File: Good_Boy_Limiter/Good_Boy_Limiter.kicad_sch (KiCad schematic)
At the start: 37 parts, among them J2 Extra General Pins, Q2 AO3422, SW3 RESET1, SW4 BOOT1, U1 ESP32-S3-WROOM-1, U2 TC4427EOA_C636891, U3 LM2576HVR-12, U8 B3B-XH-A, U9 LM393DR2G

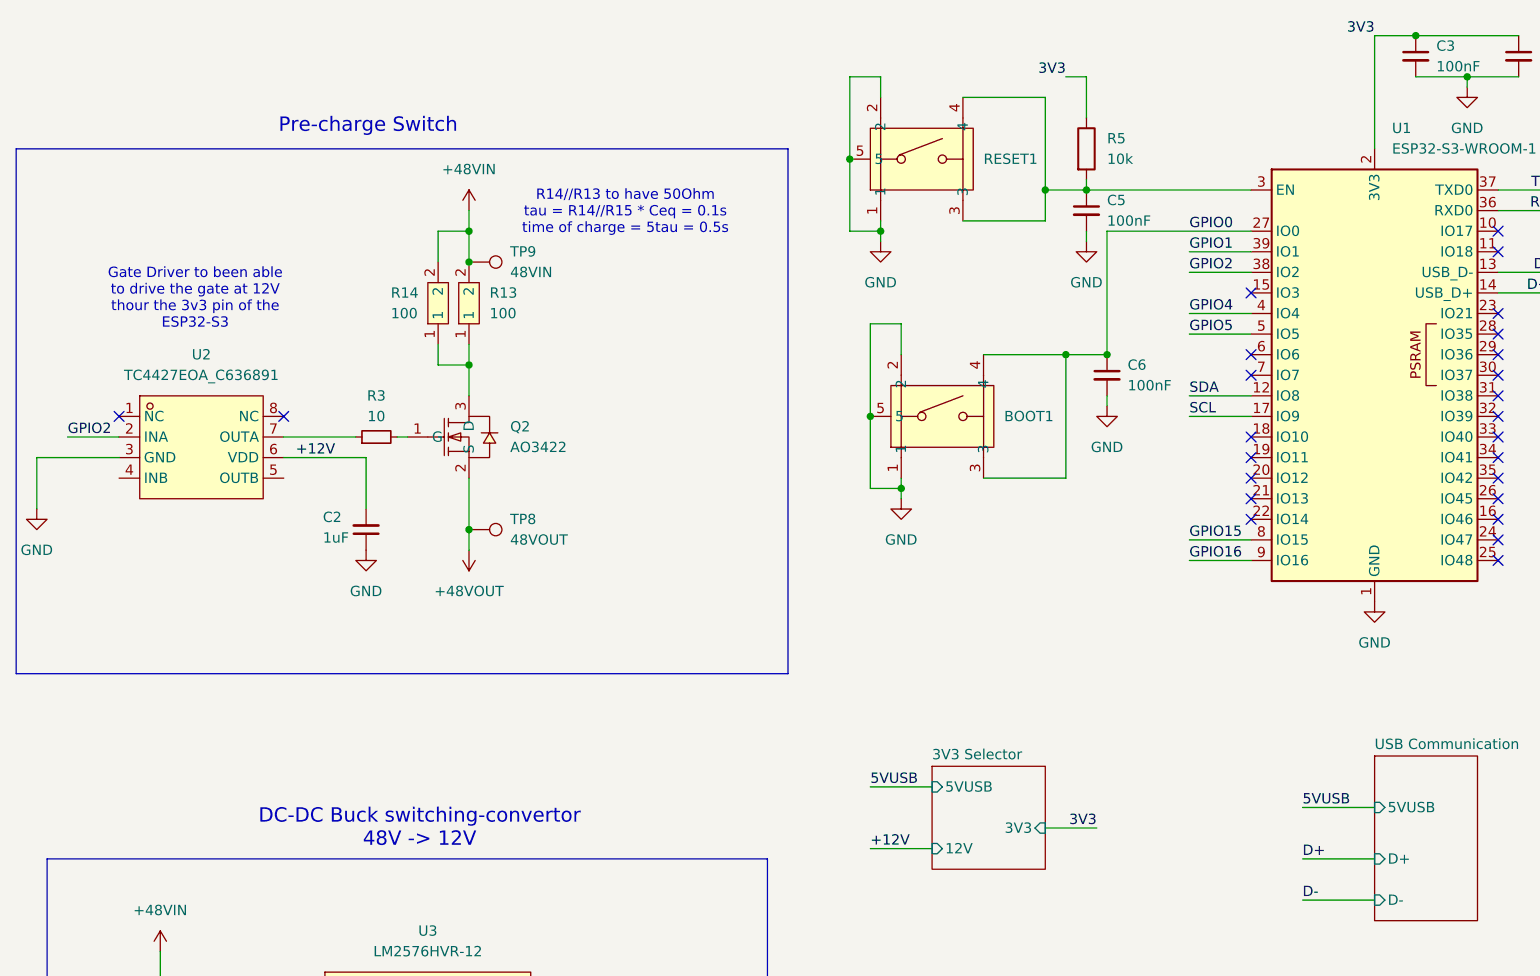
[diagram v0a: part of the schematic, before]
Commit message: Added PWR-FLag for ERC check
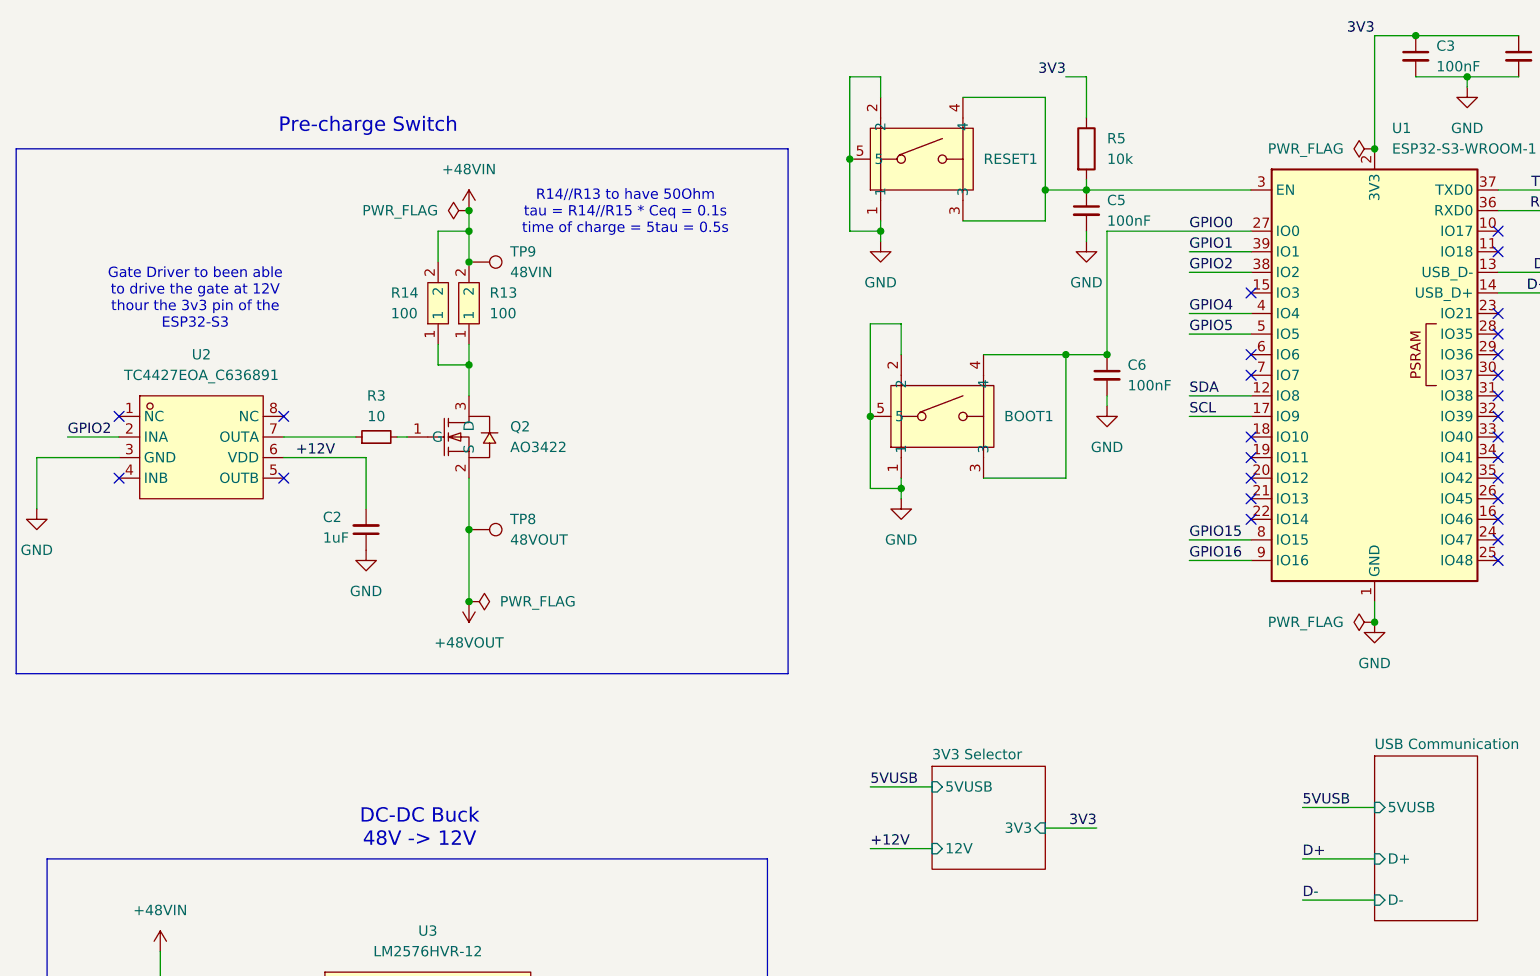
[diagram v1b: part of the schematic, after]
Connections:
- no-connect marks 26 -> 28
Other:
- note added: "DC-DC Buck 48V -> 12V"
- note removed: "DC-DC Buck switching-convertor 48V -> 12V"

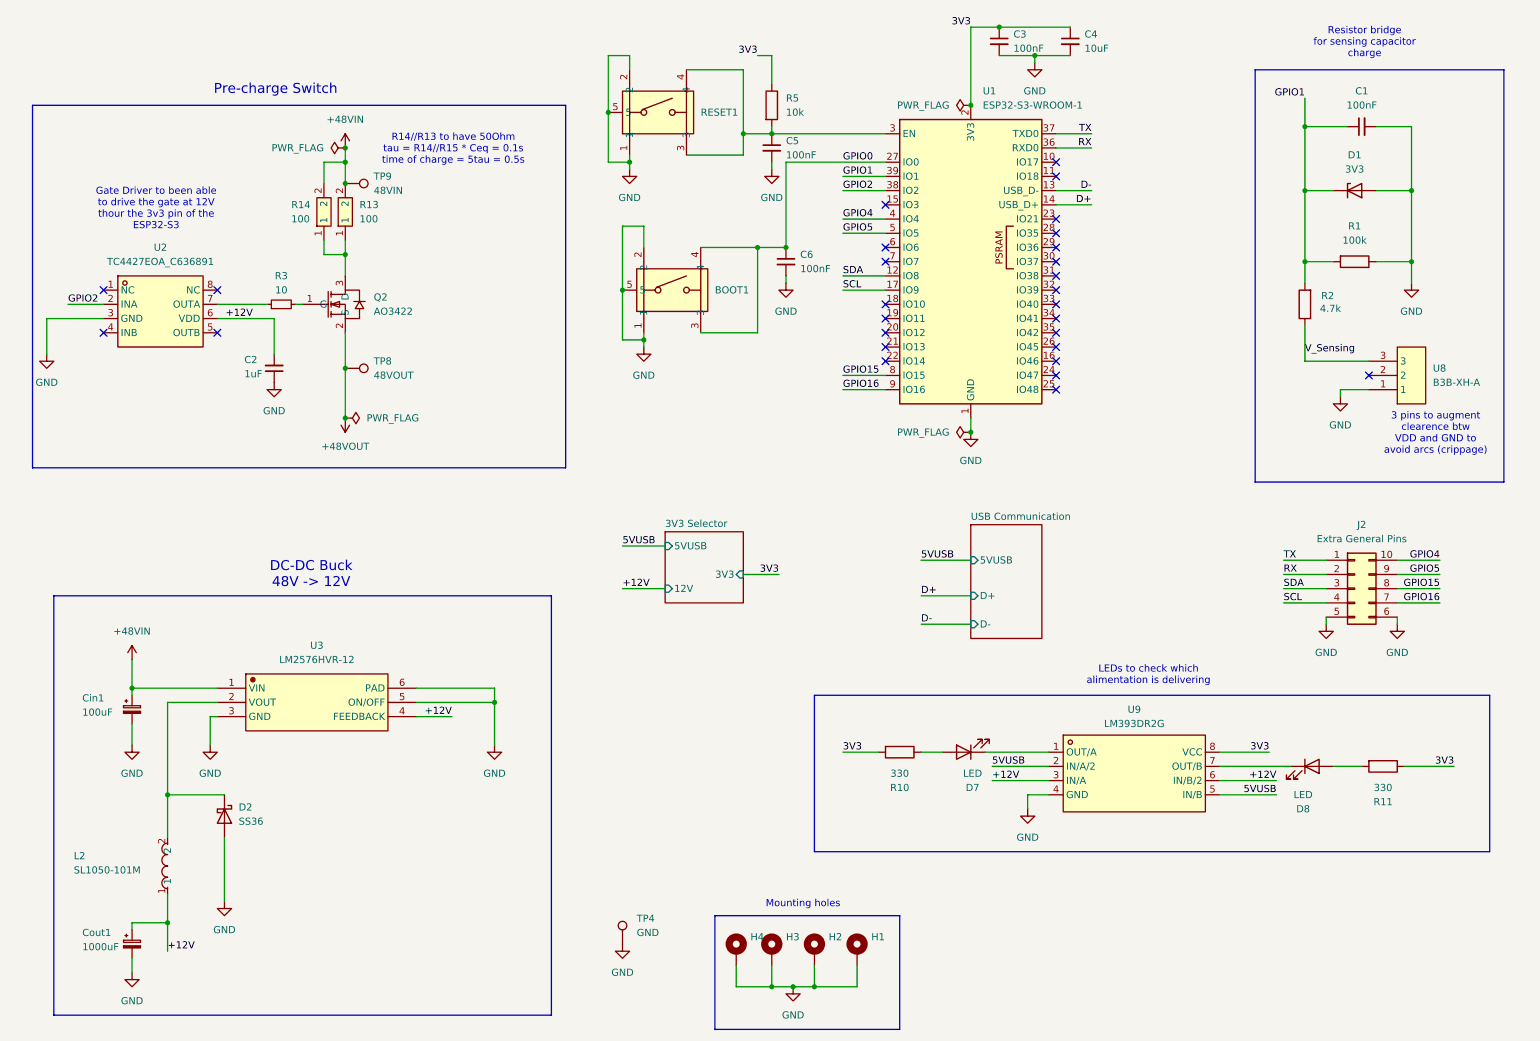
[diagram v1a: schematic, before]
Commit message: fix: added 4 voltage sensing modules to measure all the 4 PDBs
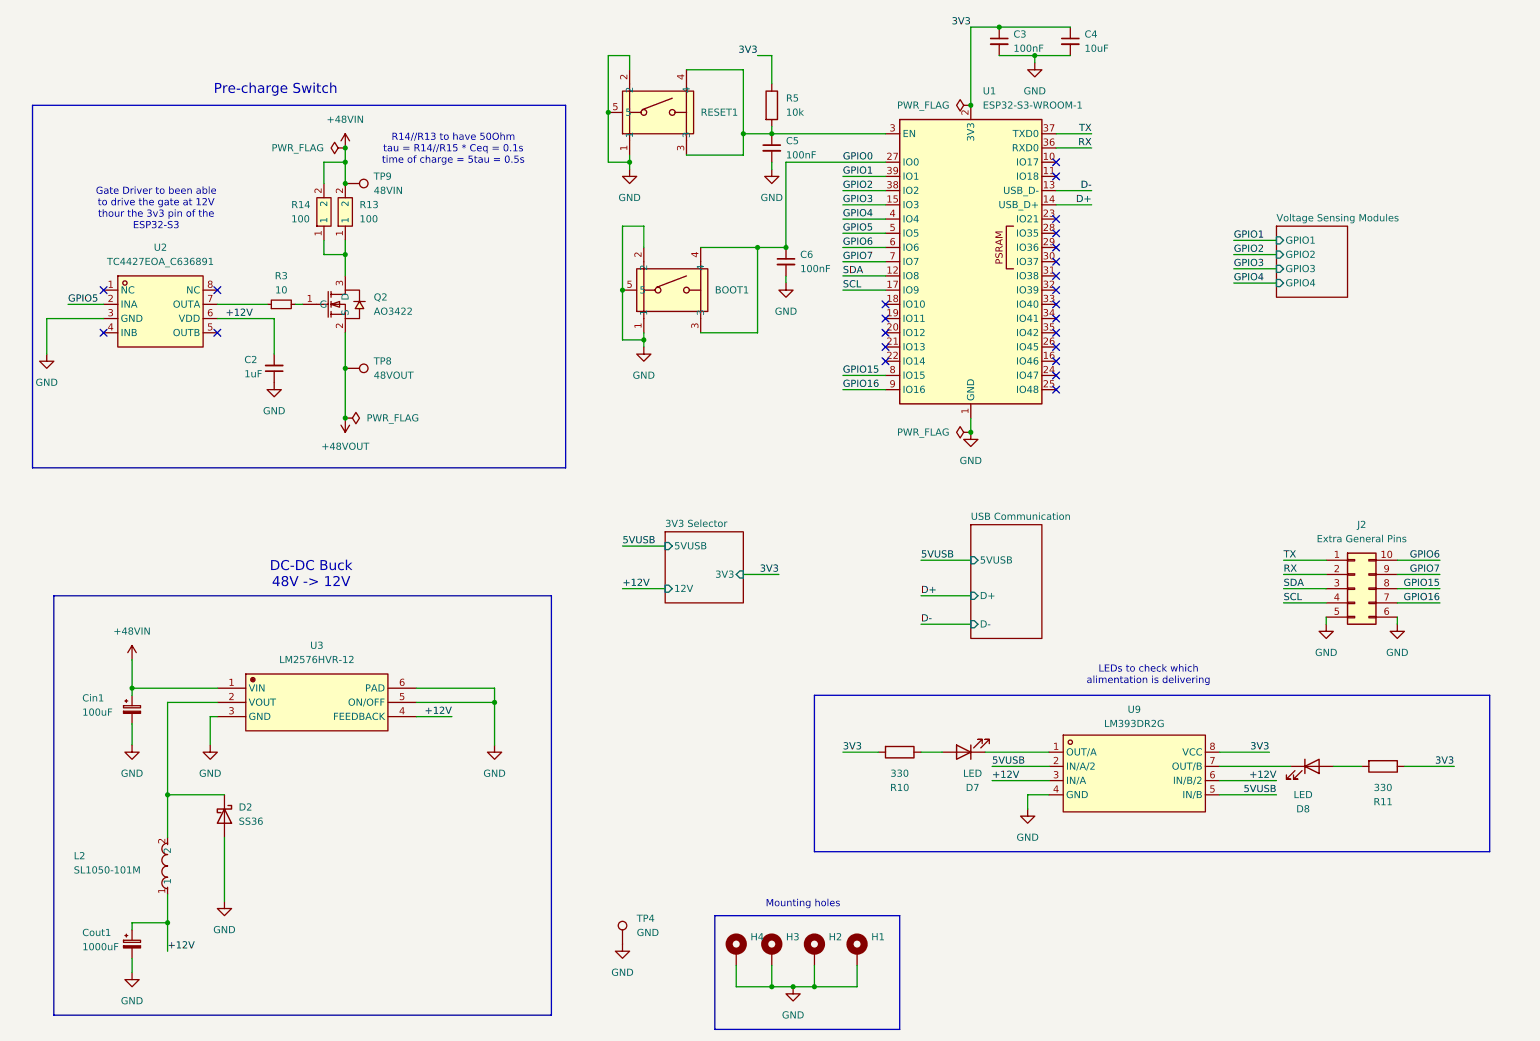
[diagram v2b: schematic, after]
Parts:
- removed C1: 100nF, Capacitor_SMD:C_0201_0603Metric_Pad0.64x0.40mm_HandSolder, symbol Device:C_Small
- removed D1: 3V3, Package_TO_SOT_SMD:SOT-23, symbol Diode:BZX84Cxx
- removed R1: 100k, Resistor_SMD:R_0603_1608Metric_Pad0.98x0.95mm_HandSolder, symbol Device:R
- removed R2: 4.7k, Resistor_SMD:R_0603_1608Metric_Pad0.98x0.95mm_HandSolder, symbol Device:R
- removed U8: B3B-XH-A, easyeda2kicad:CONN-TH_3P-P2.50_A2501WV2-3P, symbol easyeda2kicad:B3B-XH-A
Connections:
- net GPIO2: no longer U2.2 (INA)
- net GPIO4: no longer J2.10 (Pin_10)
- net GPIO5: now also U2.2 (INA); no longer J2.9 (Pin_9)
- net GPIO3: now reaches U1.15 (IO3)
- net GPIO6: now reaches U1.6 (IO6)
- net GPIO6: now also J2.10 (Pin_10)
- net GPIO7: now reaches U1.7 (IO7)
- net GPIO7: now also J2.9 (Pin_9)
- no-connect marks 28 -> 24
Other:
- added sheet Voltage Sensing Modules (vsensing_modules.kicad_sch)
- note removed: "3 pins to augment clearence btw VDD and GND to avoid arcs (crippage)"
- note removed: "Resistor bridge for sensing capacitor charge"

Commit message: Routing update
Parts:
- added R19, R20: 22, Resistor_SMD:R_0402_1005Metric, symbol Device:R_Small
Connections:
- net D+: now also R20.2; no longer U1.14 (USB_D+)
- net D-: now also R19.2; no longer U1.13 (USB_D-)
- new net: R19.1, U1.13 (USB_D-)
- new net: R20.1, U1.14 (USB_D+)
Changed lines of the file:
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@@
 	(wire
 		(pts
-			(xy 200.66 46.99) (xy 207.01 46.99)
+			(xy 200.66 46.99) (xy 209.55 46.99)
 		)
 		(stroke
@@
 	(wire
 		(pts
-			(xy 200.66 49.53) (xy 207.01 49.53)
+			(xy 200.66 49.53) (xy 209.55 49.53)
 		)
 		(stroke
@@
 	(wire
 		(pts
+			(xy 220.98 46.99) (xy 214.63 46.99)
+		)
+		(stroke
+			(width 0)
+			(type default)
+		)
+	)
+	(wire
+		(pts
 			(xy 137.16 57.15) (xy 147.32 57.15)
 		)
@@
 	(wire
 		(pts
+			(xy 220.98 49.53) (xy 214.63 49.53)
+		)
+		(stroke
+			(width 0)
+			(type default)
+		)
+	)
+	(wire
+		(pts
 			(xy 152.4 62.23) (xy 152.4 63.5)
 		)
@@
 		)
 	)
-	(label "D-"
-		(at 207.01 46.99 180)
-		(effects
-			(font
-				(size 1.27 1.27)
-			)
-			(justify right bottom)
-		)
-	)
 	(label "GPIO0"
 		(at 162.56 41.91 0)
@@
 		)
 	)
+	(label "D-"
+		(at 220.98 46.99 180)
+		(effects
+			(font
+				(size 1.27 1.27)
+			)
+			(justify right bottom)
+		)
+	)
 	(label "+12V"
 		(at 41.91 182.88 0)
@@
 		)
 	)
+	(label "D+"
+		(at 220.98 49.53 180)
+		(effects
+			(font
+				(size 1.27 1.27)
+			)
+			(justify right bottom)
+		)
+	)
 	(label "5VUSB"
 		(at 176.53 113.03 0)
@@
 		)
 	)
-	(label "D+"
-		(at 207.01 49.53 180)
-		(effects
-			(font
-				(size 1.27 1.27)
-			)
-			(justify right bottom)
-		)
-	)
 	(label "GPIO6"
 		(at 269.24 113.03 180)
@@
 	)
 	(symbol
+		(lib_id "Device:R_Small")
+		(at 212.09 46.99 90)
+		(unit 1)
+		(exclude_from_sim no)
+		(in_bom yes)
+		(on_board yes)
+		(dnp no)
+		(fields_autoplaced yes)
+		(property "Reference" "R19"
+			(at 212.09 41.91 90)
+			(effects
+				(font
+					(size 1.27 1.27)
+				)
+			)
+		)
+		(property "Value" "22"
+			(at 212.09 44.45 90)
+			(effects
+				(font
+					(size 1.27 1.27)
+				)
+			)
+		)
+		(property "Footprint" "Resistor_SMD:R_0402_1005Metric"
+			(at 212.09 46.99 0)
+			(effects
+				(font
+					(size 1.27 1.27)
+				)
+				(hide yes)
+			)
+		)
+		(property "Datasheet" "~"
+			(at 212.09 46.99 0)
+			(effects
+				(font
+					(size 1.27 1.27)
+				)
+				(hide yes)
+			)
+		)
+		(property "Description" "Resistor, small symbol"
+			(at 212.09 46.99 0)
+			(effects
+				(font
+					(size 1.27 1.27)
+				)
+				(hide yes)
+			)
+		)
+		(property "LCSC Part" "C174144"
+			(at 212.09 46.99 0)
+			(effects
+				(font
+					(size 1.27 1.27)
+				)
+				(hide yes)
+			)
+		)
+		(pin "1"
+		)
+		(pin "2"
+		)
+		(instances
+			(project "Good_Boy_Limiter"
+				(path "/e6249df1-5b78-4b75-b804-4c6c30b1afc2"
+					(reference "R19")
+					(unit 1)
+				)
+			)
+		)
+	)
+	(symbol
 		(lib_id "power:GND")
 		(at 127 74.93 0)
@@
 					(unit 1)
 				)
+			)
+		)
+	)
+	(symbol
+		(lib_id "Device:R_Small")
+		(at 212.09 49.53 90)
+		(unit 1)
+		(exclude_from_sim no)
+		(in_bom yes)
+		(on_board yes)
+		(dnp no)
+		(property "Reference" "R20"
+			(at 212.09 52.07 90)
+			(effects
+				(font
+					(size 1.27 1.27)
+				)
+			)
+		)
+		(property "Value" "22"
+			(at 212.09 54.61 90)
+			(effects
+				(font
+					(size 1.27 1.27)
+				)
+			)
+		)
+		(property "Footprint" "Resistor_SMD:R_0402_1005Metric"
+			(at 212.09 49.53 0)
+			(effects
+				(font
+					(size 1.27 1.27)
+				)
+				(hide yes)
+			)
+		)
+		(property "Datasheet" "~"
+			(at 212.09 49.53 0)
+			(effects
+				(font
+					(size 1.27 1.27)
+				)
+				(hide yes)
+			)
+		)
+		(property "Description" "Resistor, small symbol"
+			(at 212.09 49.53 0)
+			(effects
+				(font
+					(size 1.27 1.27)
+				)
+				(hide yes)
+			)
+		)
+		(property "LCSC Part" "C174144"
+			(at 212.09 49.53 0)
+			(effects
+				(font
+					(size 1.27 1.27)
+				)
+				(hide yes)
+			)
+		)
+		(pin "1"
+		)
+		(pin "2"
+		)
+		(instances
+			(project "Good_Boy_Limiter"
+				(path "/e6249df1-5b78-4b75-b804-4c6c30b1afc2"
+					(reference "R20")
+					(unit 1)
+				)

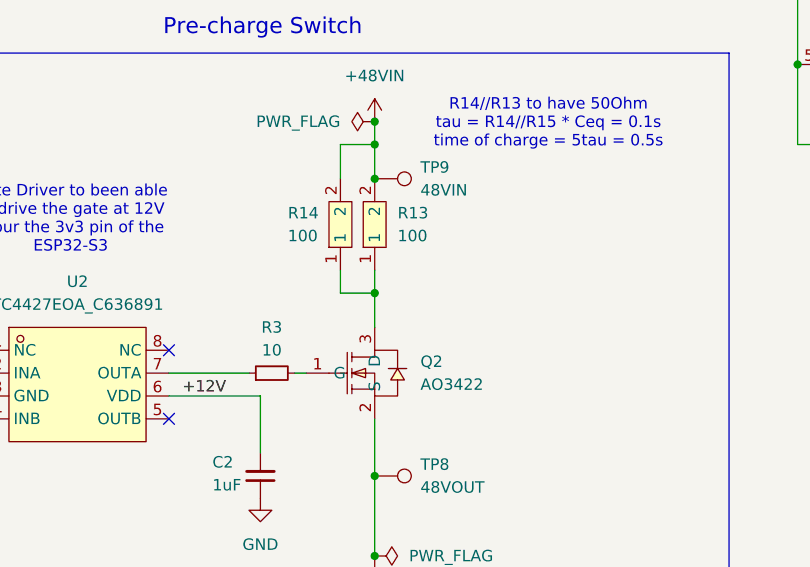
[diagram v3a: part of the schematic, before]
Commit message: More update on routing
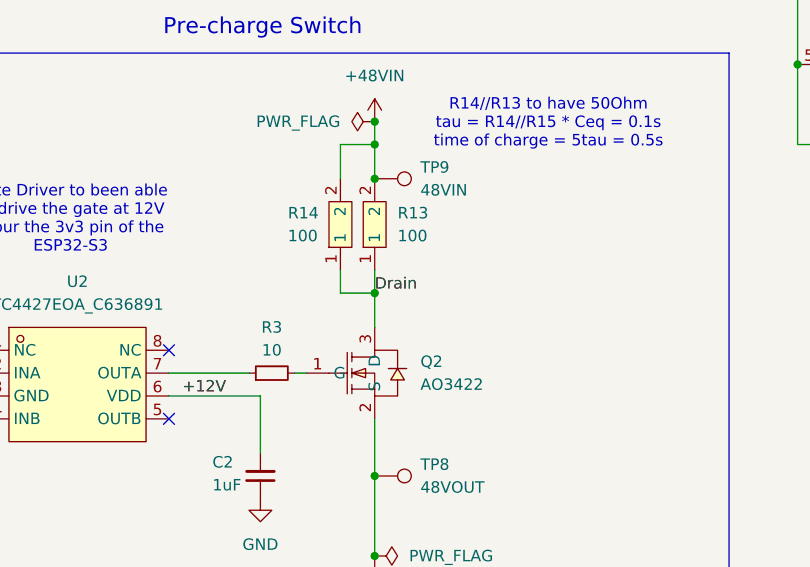
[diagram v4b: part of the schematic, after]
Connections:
- net Drain: now reaches Q2.3 (D), R13.1, R14.1
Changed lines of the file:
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@@
+		)
+	)
+	(label "Drain"
+		(at 73.66 58.42 0)
+		(effects
+			(font
+				(size 1.27 1.27)
+			)
+			(justify left bottom)
 		)
 	)
